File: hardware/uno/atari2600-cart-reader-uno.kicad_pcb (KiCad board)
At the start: 2 copper layers, 68.6 x 53.3 mm, 16 parts, among them J1 Atari 2600 Cartridge-Slot, Q1 BC327, SW1 Reset, SW2 Read, U1 MCP23017-E/SP

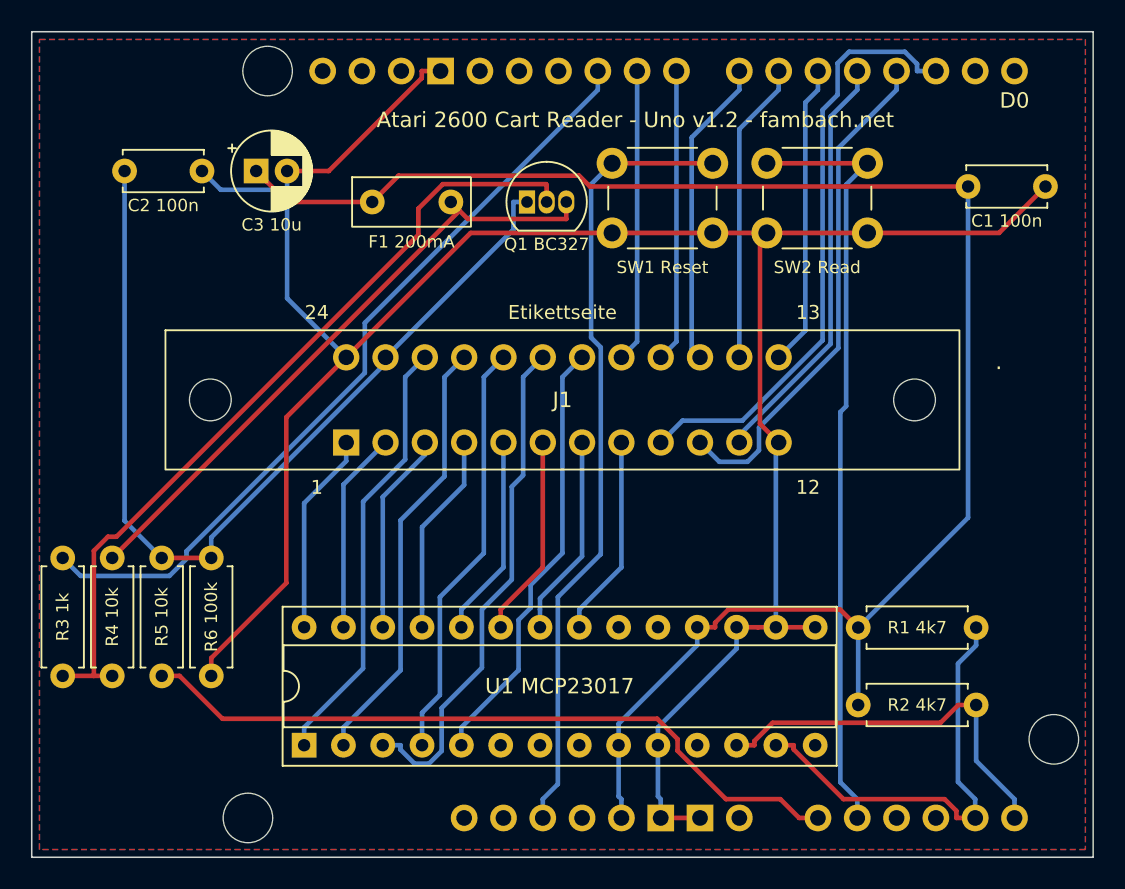
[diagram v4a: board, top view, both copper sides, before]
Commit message: Uno/Nano: address bus via two 74HC595 on SPI, MCP23017 boards kept as variants
hal.h selects the MCP23017 with #define ADDR_MCP23017.

Co-Authored-By: Claude Opus 5.5 <noreply@anthropic.com>
Claude-Session: https://claude.ai/code/session_015VQCpzuZ22TPQEmx9cLrbH
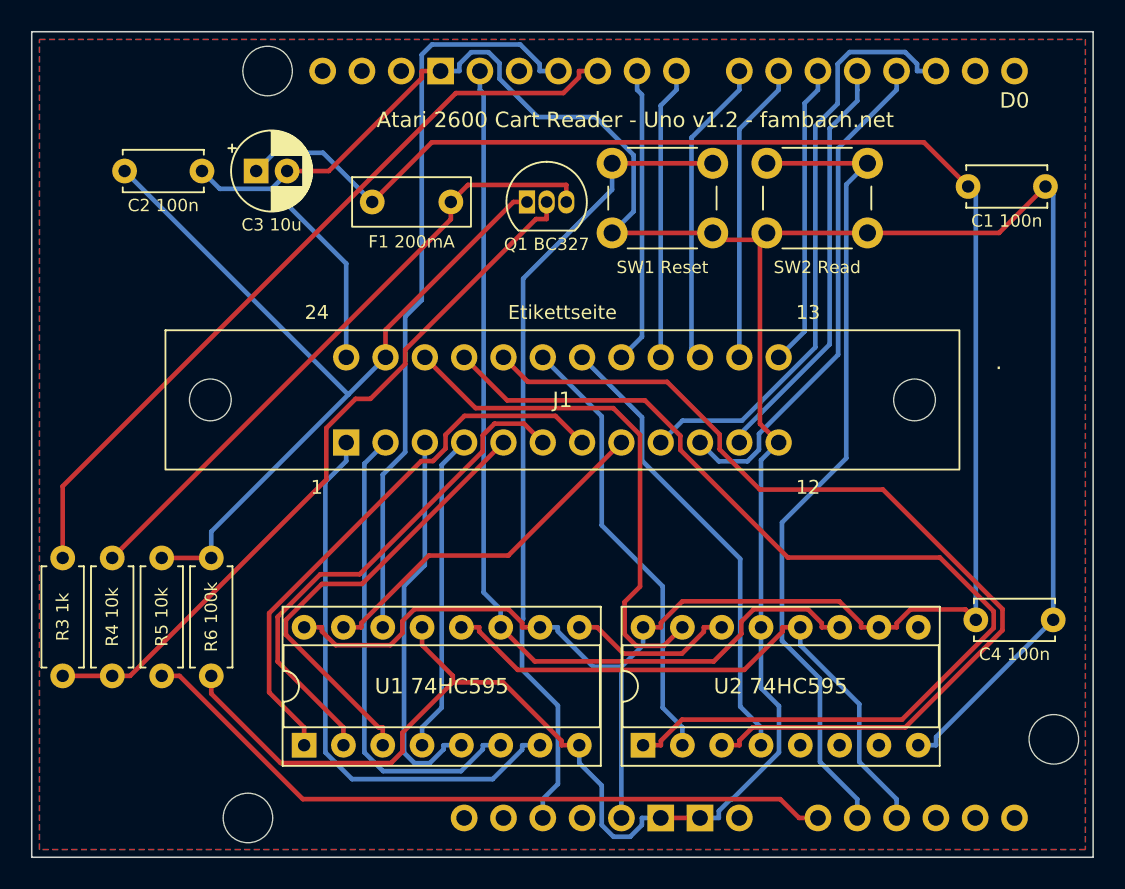
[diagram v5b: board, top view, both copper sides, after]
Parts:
- removed R1, R2: 4k7, Resistor_THT:R_Axial_DIN0207_L6.3mm_D2.5mm_P7.62mm_Horizontal
- added C4: 100n, Capacitor_THT:C_Disc_D5.0mm_W2.5mm_P5.00mm, F.Cu at (161.0, 138.0)
- added U2: 74HC595, Package_DIP:DIP-16_W7.62mm_Socket, F.Cu at (139.5, 146.1)
- U1: value MCP23017-E/SP -> 74HC595; footprint Package_DIP:DIP-28_W7.62mm_Socket -> Package_DIP:DIP-16_W7.62mm_Socket
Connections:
- A1 pad A2: (no net) -> /LATCH
- A1 pad A4: /SDA -> (no net)
- A1 pad A5: /SCL -> (no net)
- A1 pad D11: (no net) -> /MOSI
- A1 pad D13: (no net) -> /SCK
- U1 pad 1: /A8 -> /A1
- U1 pad 10: GND -> +5V
- U1 pad 11: (no net) -> /SCK
- U1 pad 12: /SCL -> /LATCH
- U1 pad 13: /SDA -> GND
- U1 pad 14: (no net) -> /MOSI
- U1 pad 15: GND -> /A0
- U1 pad 16: GND -> +5V
- U1 pad 2: /A9 -> /A2
- U1 pad 3: /A10 -> /A3
- U1 pad 4: /A11 -> /A4
- U1 pad 5: /A12 -> /A5
- U1 pad 6: (no net) -> /A6
- U1 pad 7: (no net) -> /A7
- U1 pad 8: (no net) -> GND
- U1 pad 9: +5V -> /SR_CHAIN
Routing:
- net /SCK: track 0.00 -> 61.8 mm
- net GND: track 154.8 -> 215.5 mm
- net /MOSI: track 0.00 -> 48.1 mm
- net /A9: track 28.3 -> 68.6 mm
- net /LATCH: track 0.00 -> 39.4 mm
- net /A11: track 27.2 -> 62.3 mm
- net +5V: track 110.3 -> 140.2 mm
- net /SDA: track 28.5 -> 0.00 mm
- net /SCL: track 25.0 -> 0.00 mm
- net /A7: track 13.1 -> 36.2 mm
- net /A1: track 13.1 -> 36.2 mm
- net /A2: track 13.1 -> 33.5 mm
- net /A6: track 13.1 -> 30.7 mm
- net /A3: track 13.1 -> 29.6 mm
- net /A5: track 13.1 -> 25.2 mm
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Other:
- board text added: "C4 100n"
- board text added: "U1 74HC595"
- board text added: "U2 74HC595"
- board text removed: "R1 4k7"
- board text removed: "R2 4k7"
- board text removed: "U1 MCP23017"
